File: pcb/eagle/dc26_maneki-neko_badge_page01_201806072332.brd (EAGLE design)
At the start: 75.8 x 126.7 mm, 55 parts, among them T1 RK7002BMT116, U1 STM32F030C8T, U2 PAM2301CAAB330, U3 NPTC042KFMS-RC, U5 MIC2005A-1YM5-TR, U6 MIC2005A-1YM5-TR

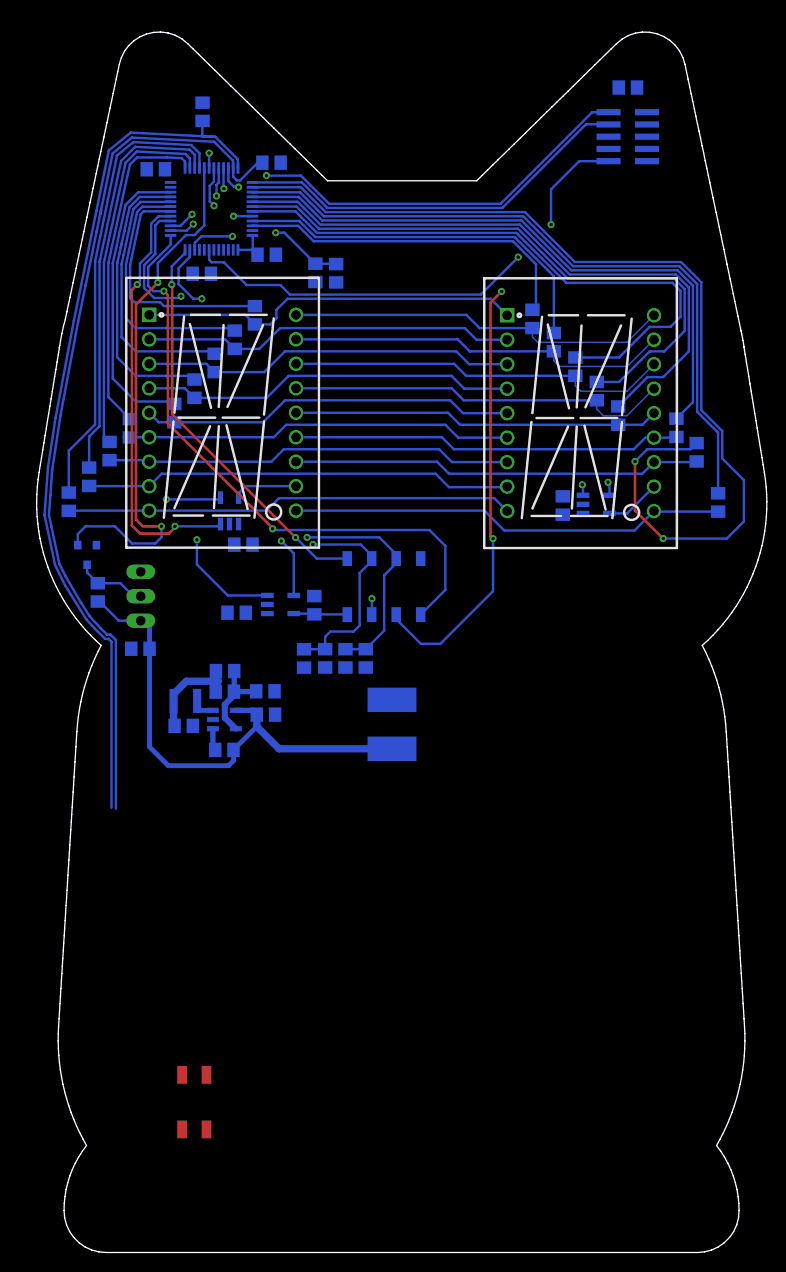
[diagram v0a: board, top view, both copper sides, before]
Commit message: finished routing incl 3v3 and gnd, except shitty addon connector (will route after artwork is added
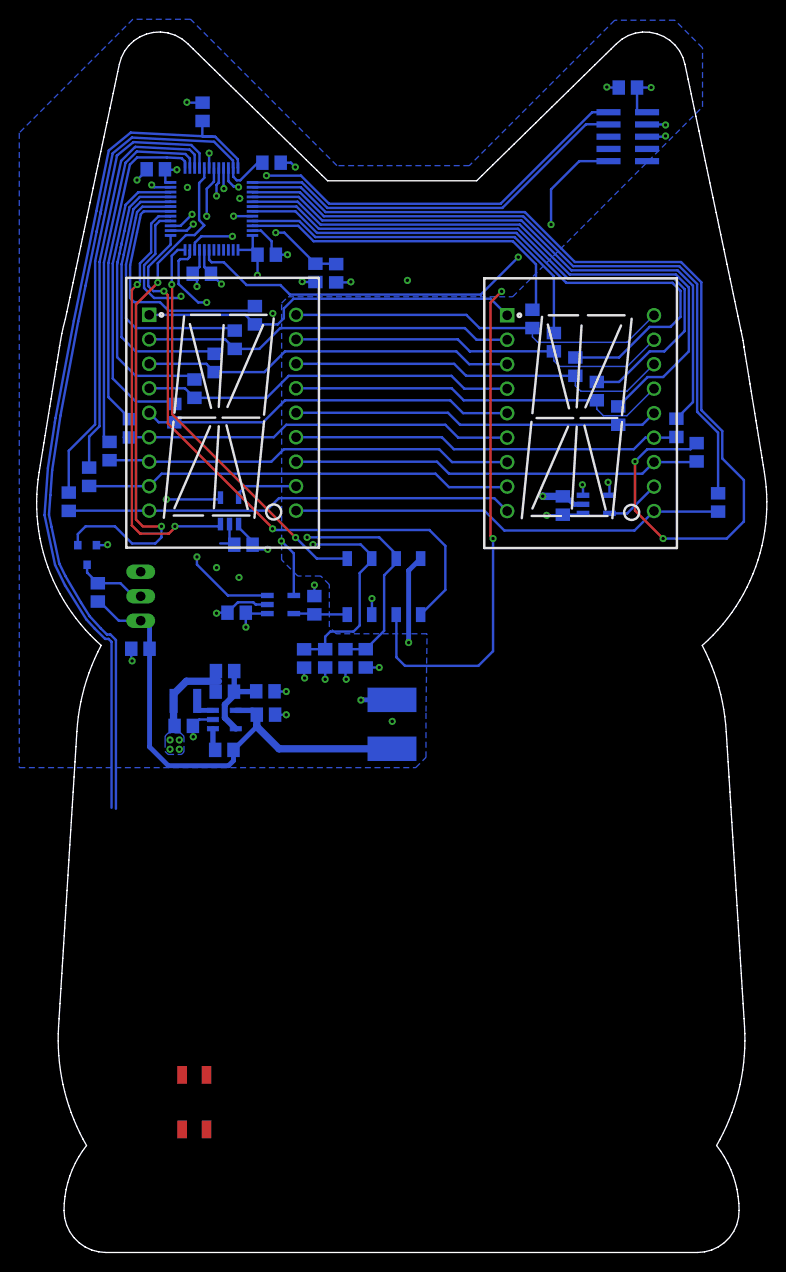
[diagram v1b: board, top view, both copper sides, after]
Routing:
- net GND: track 0.00 -> 92.9 mm, vias 0 -> 27
- net 3V3: track 12.3 -> 47.0 mm, vias 0 -> 16
- net ESP-CH_PD: track 80.8 -> 89.1 mm
- net ESP-EN: track 71.9 -> 69.5 mm
- net EYE-RIGHT-EN: track 72.3 -> 70.6 mm
- added copper zone on layer 15, net 3V3
- added copper zone on layer 16, net 3V3
- added copper zone on layer 16, net GND
- added copper zone on layer 2, net GND
